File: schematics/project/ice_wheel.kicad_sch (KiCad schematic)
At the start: 2 parts, among them U1 OPA320xxDBV, U2 Teensy4.1

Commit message: Structure of schematics
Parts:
- removed U1: OPA320xxDBV, Package_TO_SOT_SMD:SOT-23-5, symbol Amplifier_Operational:OPA330xxDBV
- removed U2: Teensy4.1, teensy:Teensy41, symbol teensy:Teensy4.1
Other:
- added sheet Battery Management System (batmansys.kicad_sch)
- added sheet Bluetooth (bluetooth.kicad_sch)
- added sheet Misc (misc.kicad_sch)
- added sheet Motor Controller (motorController.kicad_sch)
- added sheet Prop Shield (propshield.kicad_sch)
- added sheet Teensy (teensy.kicad_sch)

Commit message: First steps with kicad structure -> kinda sucks
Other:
- sheet Prop Shield ports: added {I2C_Motion}, {SPI_PS}; removed I2C_Motion, SPI_propshield
- sheet Teensy ports: added {I2C_Motion}, {SPI_PS}; removed I2C_Motion, SPI_propshield

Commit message: some progress, dust slowly clears
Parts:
- added J1: Conn_01x02, Connector_JST:JST_SHL_SM02B-SHLS-TF_1x02-1MP_P1.00mm_Horizontal, symbol Connector_Generic:Conn_01x02
- added J2: Conn_01x02, symbol Connector_Generic:Conn_01x02
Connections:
- new net +48V: J2.1 (Pin_1)
- new net +5P: J1.1 (Pin_1)
- new net GND: J1.2 (Pin_2)
- new net GNDPWR: J2.2 (Pin_2)
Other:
- sheet Bluetooth ports: added Bluetooth; removed bt_rx, bt_tx
- sheet Motor Controller ports: added hallSensor; removed hallSensors
- sheet Teensy ports: added Bluetooth, footpad_a , hallSensor; removed bt_rx, bt_tx, hallSensors
- note added: "5V Input"

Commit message: small progress, angsthasen
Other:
- sheet Misc ports: added Speaker, poti_IN; removed none
- sheet Motor Controller ports: added throttle_pwm; removed throttle_a
- sheet Prop Shield ports: added Speaker; removed none
- sheet Teensy ports: added poti_IN; removed throttle_a
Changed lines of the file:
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@@
+    (stroke (width 0) (type default) (color 0 0 0 0))
+  )
+  (bus (pts (xy 161.29 73.66) (xy 161.29 80.01))
     (stroke (width 0) (type default) (color 0 0 0 0))
   )
@@
     (stroke (width 0) (type default) (color 0 0 0 0))
   )
-  (wire (pts (xy 153.67 107.95) (xy 166.37 107.95))
+  (wire (pts (xy 153.67 82.55) (xy 166.37 82.55))
+    (stroke (width 0) (type default) (color 0 0 0 0))
+  )
+  (bus (pts (xy 102.87 73.66) (xy 161.29 73.66))
     (stroke (width 0) (type default) (color 0 0 0 0))
   )
@@
     (stroke (width 0) (type default) (color 0 0 0 0))
   )
+  (bus (pts (xy 102.87 80.01) (xy 102.87 73.66))
+    (stroke (width 0) (type default) (color 0 0 0 0))
+  )
   (wire (pts (xy 69.85 27.94) (xy 69.85 30.48))
     (stroke (width 0) (type default) (color 0 0 0 0))
   )
+  (bus (pts (xy 96.52 80.01) (xy 102.87 80.01))
+    (stroke (width 0) (type default) (color 0 0 0 0))
+  )
   (wire (pts (xy 96.52 106.68) (xy 109.22 106.68))
     (stroke (width 0) (type default) (color 0 0 0 0))
@@
     (stroke (width 0) (type default) (color 0 0 0 0))
   )
+  (bus (pts (xy 161.29 80.01) (xy 166.37 80.01))
+    (stroke (width 0) (type default) (color 0 0 0 0))
+  )
+  (bus (pts (xy 153.67 107.95) (xy 166.37 107.95))
+    (stroke (width 0) (type default) (color 0 0 0 0))
+  )
   (wire (pts (xy 68.58 55.88) (xy 71.12 55.88))
     (stroke (width 0) (type default) (color 0 0 0 0))
   )
   (wire (pts (xy 72.39 25.4) (xy 69.85 25.4))
-    (stroke (width 0) (type default) (color 0 0 0 0))
-  )
-  (bus (pts (xy 153.67 80.01) (xy 166.37 80.01))
     (stroke (width 0) (type default) (color 0 0 0 0))
   )
@@
       (effects (font (size 1.27 1.27)) (justify right))
     )
+    (pin "Speaker" output (at 96.52 80.01 0)
+      (effects (font (size 1.27 1.27)) (justify right))
+    )
   )
   (sheet (at 166.37 127) (size 43.18 22.86) (fields_autoplaced)
@@
     )
   )
-  (sheet (at 166.37 77.47) (size 40.64 11.43) (fields_autoplaced)
+  (sheet (at 166.37 105.41) (size 40.64 11.43) (fields_autoplaced)
     (stroke (width 0.1524) (type solid) (color 0 0 0 0))
     (fill (color 0 0 0 0.0000))
-    (property "Sheet name" "Bluetooth" (id 0) (at 166.37 76.7584 0)
+    (property "Sheet name" "Bluetooth" (id 0) (at 166.37 104.6984 0)
       (effects (font (size 1.27 1.27)) (justify left bottom))
     )
-    (property "Sheet file" "bluetooth.kicad_sch" (id 1) (at 166.37 89.4846 0)
+    (property "Sheet file" "bluetooth.kicad_sch" (id 1) (at 166.37 117.4246 0)
       (effects (font (size 1.27 1.27)) (justify left top))
     )
-    (pin "Bluetooth" bidirectional (at 166.37 80.01 180)
+    (pin "Bluetooth" bidirectional (at 166.37 107.95 180)
       (effects (font (size 1.27 1.27)) (justify left))
     )
@@
       (effects (font (size 1.27 1.27)) (justify left))
     )
-    (pin "throttle_a" input (at 109.22 106.68 180)
-      (effects (font (size 1.27 1.27)) (justify left))
-    )
     (pin "lowPoBreak" input (at 109.22 119.38 180)
       (effects (font (size 1.27 1.27)) (justify left))
@@
       (effects (font (size 1.27 1.27)) (justify left))
     )
-    (pin "Bluetooth" bidirectional (at 153.67 80.01 0)
-      (effects (font (size 1.27 1.27)) (justify right))
-    )
-    (pin "footpad_a " input (at 153.67 107.95 0)
+    (pin "Bluetooth" bidirectional (at 153.67 107.95 0)
+      (effects (font (size 1.27 1.27)) (justify right))
+    )
+    (pin "footpad_a " input (at 153.67 82.55 0)
       (effects (font (size 1.27 1.27)) (justify right))
     )
     (pin "RS485_BMS" bidirectional (at 153.67 132.08 0)
       (effects (font (size 1.27 1.27)) (justify right))
+    )
+    (pin "poti_IN" input (at 109.22 106.68 180)
+      (effects (font (size 1.27 1.27)) (justify left))
     )
   )
@@
       (effects (font (size 1.27 1.27)) (justify right))
     )
-    (pin "throttle_a" input (at 96.52 106.68 0)
-      (effects (font (size 1.27 1.27)) (justify right))
-    )
     (pin "cruise" input (at 96.52 116.84 0)
       (effects (font (size 1.27 1.27)) (justify right))
@@
       (effects (font (size 1.27 1.27)) (justify right))
     )
-  )
-  (sheet (at 166.37 104.14) (size 25.4 10.16) (fields_autoplaced)
+    (pin "throttle_pwm" input (at 96.52 106.68 0)
+      (effects (font (size 1.27 1.27)) (justify right))
+    )
+  )
+  (sheet (at 166.37 77.47) (size 26.67 17.78) (fields_autoplaced)
     (stroke (width 0.1524) (type solid) (color 0 0 0 0))
     (fill (color 0 0 0 0.0000))
-    (property "Sheet name" "Misc" (id 0) (at 166.37 103.4284 0)
+    (property "Sheet name" "Misc" (id 0) (at 166.37 76.7584 0)
       (effects (font (size 1.27 1.27)) (justify left bottom))
     )
-    (property "Sheet file" "misc.kicad_sch" (id 1) (at 166.37 114.8846 0)
+    (property "Sheet file" "misc.kicad_sch" (id 1) (at 166.37 95.8346 0)
       (effects (font (size 1.27 1.27)) (justify left top))
     )
-    (pin "footpad_a " output (at 166.37 107.95 180)
+    (pin "footpad_a " output (at 166.37 82.55 180)
+      (effects (font (size 1.27 1.27)) (justify left))
+    )
+    (pin "Speaker" input (at 166.37 80.01 180)
+      (effects (font (size 1.27 1.27)) (justify left))
+    )
+    (pin "poti_IN" output (at 166.37 85.09 180)
       (effects (font (size 1.27 1.27)) (justify left))
     )
@@
       (reference "#PWR0137") (unit 1) (value "GND") (footprint "")
     )
+    (path "/a8032040-4653-49ee-95a3-c7cb36f467f5/990c3227-f66d-46f5-aa84-bd643388a276"
+      (reference "#PWR0138") (unit 1) (value "GND") (footprint "")
+    )
+    (path "/a8032040-4653-49ee-95a3-c7cb36f467f5/e02e4906-3c35-41b7-aaaa-ae3e3959c322"
+      (reference "#PWR0139") (unit 1) (value "+3V3") (footprint "")
+    )
+    (path "/a8032040-4653-49ee-95a3-c7cb36f467f5/f23605ae-8089-497b-a870-9c2ec8b93d03"
+      (reference "#PWR0140") (unit 1) (value "GND") (footprint "")
+    )
+    (path "/e60c338a-4f31-4486-88a3-b5454f96f251/5bd1a448-8ecc-4687-9ec0-737093a96f28"
+      (reference "#PWR0141") (unit 1) (value "GND") (footprint "")
+    )
+    (path "/e60c338a-4f31-4486-88a3-b5454f96f251/6c598751-03ec-42b5-8fe1-611876748d01"
+      (reference "#PWR0142") (unit 1) (value "+5V") (footprint "")
+    )
+    (path "/e60c338a-4f31-4486-88a3-b5454f96f251/c7b52073-3a92-4836-95ba-e712423fa30b"
+      (reference "#PWR0143") (unit 1) (value "GND") (footprint "")
+    )
+    (path "/e60c338a-4f31-4486-88a3-b5454f96f251/794c5c5e-371a-4787-81c1-a38c0fd636c6"
+      (reference "#PWR0144") (unit 1) (value "+5V") (footprint "")
+    )
+    (path "/e60c338a-4f31-4486-88a3-b5454f96f251/547e0894-6a74-49e9-9348-41865fbacb74"
+      (reference "#PWR0145") (unit 1) (value "GND") (footprint "")
+    )
+    (path "/e60c338a-4f31-4486-88a3-b5454f96f251/7bcb3274-ffad-47ba-85fa-1ec40074f0bc"
+      (reference "#PWR0146") (unit 1) (value "+5V") (footprint "")
+    )
     (path "/e170b43f-4cff-4505-8548-8011a1acf870/0a5cbc8c-d3cc-44f1-bc1d-4f5ea60978a2/654a37c9-46df-4b82-9933-5b4bab00a4da"
       (reference "C1") (unit 1) (value "C") (footprint "Capacitor_SMD:C_0603_1608Metric")
@@
       (reference "J2") (unit 1) (value "Conn_01x02") (footprint "")
     )
+    (path "/e60c338a-4f31-4486-88a3-b5454f96f251/c1085153-8f02-438d-ba95-d4b7d78aa733"
+      (reference "J3") (unit 1) (value "Conn_01x06") (footprint "")
+    )
+    (path "/e60c338a-4f31-4486-88a3-b5454f96f251/d6d0d868-e525-4399-bd4b-858390f2d3e6"
+      (reference "J4") (unit 1) (value "Conn_01x02") (footprint "")
+    )
     (path "/e170b43f-4cff-4505-8548-8011a1acf870/d87a0ee4-8016-40e3-98eb-7d78f313da4f"
       (reference "Q1") (unit 1) (value "BSS123") (footprint "Package_TO_SOT_SMD:SOT-23")
@@
     )
     (path "/e170b43f-4cff-4505-8548-8011a1acf870/8f7d1028-dc21-43d9-87a1-de994e1d134c"
-      (reference "R4") (unit 1) (value "R") (footprint "Resistor_SMD:R_0603_1608Metric")
+      (reference "R4") (unit 1) (value "1k") (footprint "Resistor_SMD:R_0603_1608Metric")
     )
     (path "/e170b43f-4cff-4505-8548-8011a1acf870/d7faf8fe-7d8a-426a-8274-194ddfcfaf5e"
-      (reference "R5") (unit 1) (value "R") (footprint "Resistor_SMD:R_0603_1608Metric")
+      (reference "R5") (unit 1) (value "1k") (footprint "Resistor_SMD:R_0603_1608Metric")
     )
     (path "/e170b43f-4cff-4505-8548-8011a1acf870/bcf35816-9bc9-4f6a-808b-350c85f525e7"
-      (reference "R6") (unit 1) (value "R") (footprint "Resistor_SMD:R_0603_1608Metric")
+      (reference "R6") (unit 1) (value "1k") (footprint "Resistor_SMD:R_0603_1608Metric")
     )
     (path "/e170b43f-4cff-4505-8548-8011a1acf870/cc39c052-37ed-400c-8ee6-c721ba66d828"
@@
       (reference "R13") (unit 1) (value "R") (footprint "Resistor_SMD:R_0603_1608Metric")
     )
+    (path "/e60c338a-4f31-4486-88a3-b5454f96f251/333792e1-5d2d-49b9-9ea6-0ab44501b72f"
+      (reference "RV1") (unit 1) (value "TC33X-1-203E") (footprint "Potentiometer_SMD:Potentiometer_Bourns_TC33X_Vertical")
+    )
+    (path "/e60c338a-4f31-4486-88a3-b5454f96f251/374f140d-5a1d-4c15-ab47-7f9415d6c4df"
+      (reference "RV2") (unit 1) (value "TC33X-1-203E") (footprint "Potentiometer_SMD:Potentiometer_Bourns_TC33X_Vertical")
+    )
+    (path "/e60c338a-4f31-4486-88a3-b5454f96f251/51914a10-e4f2-4520-870e-efe886085592"
+      (reference "RV3") (unit 1) (value "TC33X-1-203E") (footprint "Potentiometer_SMD:Potentiometer_Bourns_TC33X_Vertical")
+    )
     (path "/a8032040-4653-49ee-95a3-c7cb36f467f5/dd35ef3b-164d-4c70-932a-8e4d423737d2"

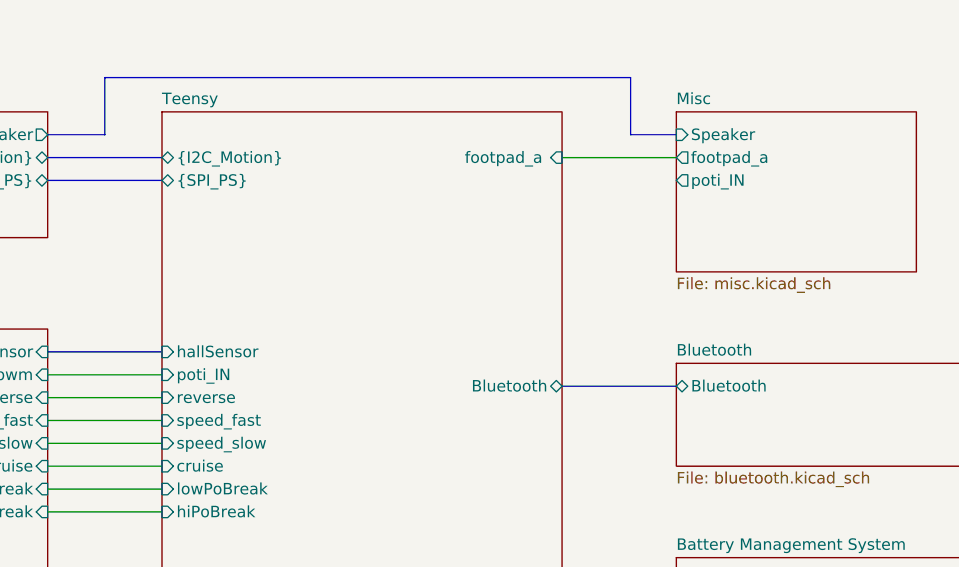
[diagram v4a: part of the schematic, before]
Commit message: Adding separate library, BT Module
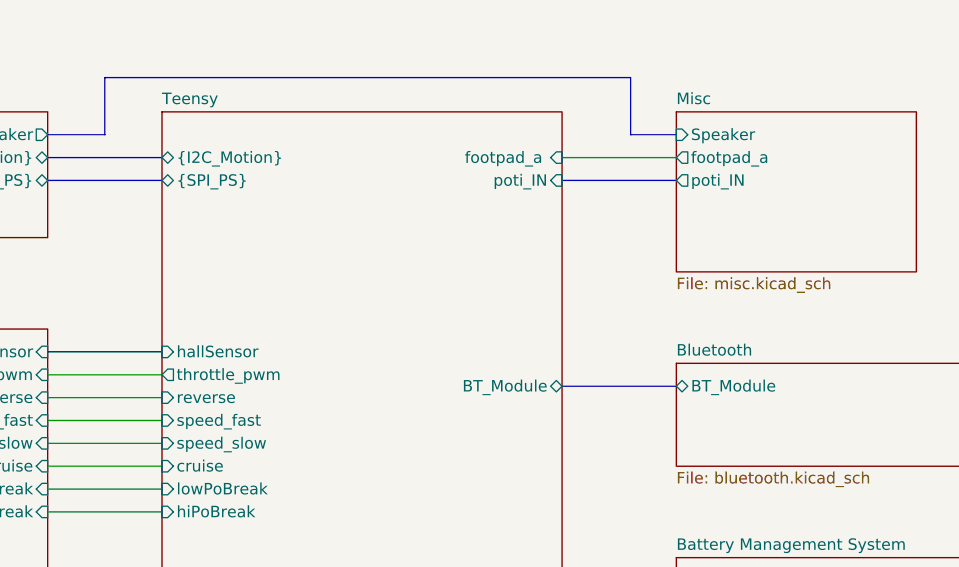
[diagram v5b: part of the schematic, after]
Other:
- sheet Bluetooth ports: added BT_Module; removed Bluetooth
- sheet Teensy ports: added BT_Module, throttle_pwm; removed Bluetooth

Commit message: random commit
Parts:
- J1: footprint Connector_JST:JST_SHL_SM02B-SHLS-TF_1x02-1MP_P1.00mm_Horizontal -> Connector_Phoenix_MSTB:PhoenixContact_MSTBA_2,5_2-G-5,08_1x02_P5.08mm_Horizontal
- J2: footprint (none) -> Connector_Phoenix_MSTB:PhoenixContact_MSTBA_2,5_2-G-5,08_1x02_P5.08mm_Horizontal
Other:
- sheet Misc ports: added analog_reserve, digital_reserve; removed none
- sheet Teensy ports: added analog_reserve, digital_reserve; removed none
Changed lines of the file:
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@@
+    (stroke (width 0) (type default) (color 0 0 0 0))
+  )
+  (bus (pts (xy 153.67 90.17) (xy 166.37 90.17))
     (stroke (width 0) (type default) (color 0 0 0 0))
   )
@@
   )
   (wire (pts (xy 69.85 25.4) (xy 69.85 22.86))
+    (stroke (width 0) (type default) (color 0 0 0 0))
+  )
+  (bus (pts (xy 153.67 87.63) (xy 166.37 87.63))
     (stroke (width 0) (type default) (color 0 0 0 0))
   )
@@
       (effects (font (size 1.27 1.27)) (justify left))
     )
-    (property "Footprint" "" (id 2) (at 77.47 25.4 0)
+    (property "Footprint" "Connector_Phoenix_MSTB:PhoenixContact_MSTBA_2,5_2-G-5,08_1x02_P5.08mm_Horizontal" (id 2) (at 77.47 25.4 0)
       (effects (font (size 1.27 1.27)) hide)
     )
@@
       (effects (font (size 1.27 1.27)) (justify left))
     )
-    (property "Footprint" "Connector_JST:JST_SHL_SM02B-SHLS-TF_1x02-1MP_P1.00mm_Horizontal" (id 2) (at 76.2 53.34 0)
+    (property "Footprint" "Connector_Phoenix_MSTB:PhoenixContact_MSTBA_2,5_2-G-5,08_1x02_P5.08mm_Horizontal" (id 2) (at 76.2 53.34 0)
       (effects (font (size 1.27 1.27)) hide)
     )
@@
       (effects (font (size 1.27 1.27)) (justify right))
     )
+    (pin "digital_reserve" bidirectional (at 153.67 87.63 0)
+      (effects (font (size 1.27 1.27)) (justify right))
+    )
+    (pin "analog_reserve" bidirectional (at 153.67 90.17 0)
+      (effects (font (size 1.27 1.27)) (justify right))
+    )
   )
   (sheet (at 67.31 101.6) (size 29.21 48.26) (fields_autoplaced)
@@
     )
     (pin "poti_IN" output (at 166.37 85.09 180)
+      (effects (font (size 1.27 1.27)) (justify left))
+    )
+    (pin "analog_reserve" bidirectional (at 166.37 90.17 180)
+      (effects (font (size 1.27 1.27)) (justify left))
+    )
+    (pin "digital_reserve" bidirectional (at 166.37 87.63 180)
       (effects (font (size 1.27 1.27)) (justify left))
     )
@@
     )
     (path "/e170b43f-4cff-4505-8548-8011a1acf870/fd47a1e5-df7e-4eee-a276-aa165209f13d"
-      (reference "#PWR?") (unit 1) (value "+48V") (footprint "")
+      (reference "#PWR0148") (unit 1) (value "+48V") (footprint "")
+    )
+    (path "/e60c338a-4f31-4486-88a3-b5454f96f251/787500e1-f92b-4a71-91ed-aadf5df66a1a"
+      (reference "#PWR0149") (unit 1) (value "GND") (footprint "")
+    )
+    (path "/e60c338a-4f31-4486-88a3-b5454f96f251/71b3e57e-4aff-4ae1-b69e-3eadce93f575"
+      (reference "#PWR0150") (unit 1) (value "GND") (footprint "")
     )
     (path "/e170b43f-4cff-4505-8548-8011a1acf870/0a5cbc8c-d3cc-44f1-bc1d-4f5ea60978a2/654a37c9-46df-4b82-9933-5b4bab00a4da"
@@
       (reference "D6") (unit 1) (value "D3V3S1U2LP1610-7") (footprint "Diode_SMD:D_0603_1608Metric_Pad1.05x0.95mm_HandSolder")
     )
+    (path "/e60c338a-4f31-4486-88a3-b5454f96f251/848f00ae-2b51-4a13-ba2b-b1d2cf17c1a6"
+      (reference "D7") (unit 1) (value "D3V3S1U2LP1610-7") (footprint "Diode_SMD:D_0603_1608Metric_Pad1.05x0.95mm_HandSolder")
+    )
+    (path "/e60c338a-4f31-4486-88a3-b5454f96f251/d1560112-0392-430e-8f8c-a61a68a9e881"
+      (reference "D8") (unit 1) (value "D3V3S1U2LP1610-7") (footprint "Diode_SMD:D_0603_1608Metric_Pad1.05x0.95mm_HandSolder")
+    )
     (path "/da0d5712-30e0-4d75-a17b-09a309cdb0af"
-      (reference "J1") (unit 1) (value "Conn_01x02") (footprint "Connector_JST:JST_SHL_SM02B-SHLS-TF_1x02-1MP_P1.00mm_Horizontal")
+      (reference "J1") (unit 1) (value "Conn_01x02") (footprint "Connector_Phoenix_MSTB:PhoenixContact_MSTBA_2,5_2-G-5,08_1x02_P5.08mm_Horizontal")
     )
     (path "/510d7d1a-ff03-4dad-9887-a4cfb9760797"
-      (reference "J2") (unit 1) (value "Conn_01x02") (footprint "")
+      (reference "J2") (unit 1) (value "Conn_01x02") (footprint "Connector_Phoenix_MSTB:PhoenixContact_MSTBA_2,5_2-G-5,08_1x02_P5.08mm_Horizontal")
     )
     (path "/e60c338a-4f31-4486-88a3-b5454f96f251/c1085153-8f02-438d-ba95-d4b7d78aa733"
-      (reference "J3") (unit 1) (value "Conn_01x06") (footprint "")
+      (reference "J3") (unit 1) (value "Conn_01x06") (footprint "Connector_JST:JST_SH_SM06B-SRSS-TB_1x06-1MP_P1.00mm_Horizontal")
     )
     (path "/e60c338a-4f31-4486-88a3-b5454f96f251/d6d0d868-e525-4399-bd4b-858390f2d3e6"
-      (reference "J4") (unit 1) (value "Conn_01x02") (footprint "")
+      (reference "J4") (unit 1) (value "Conn_01x02") (footprint "Connector_JST:JST_SHL_SM02B-SHLS-TF_1x02-1MP_P1.00mm_Horizontal")
     )
     (path "/e60c338a-4f31-4486-88a3-b5454f96f251/e31a5680-510d-4c8b-a1a2-e25dc53ad7a6"
-      (reference "J5") (unit 1) (value "Conn_01x03") (footprint "")
+      (reference "J5") (unit 1) (value "Conn_01x03") (footprint "Connector_JST:JST_SH_SM03B-SRSS-TB_1x03-1MP_P1.00mm_Horizontal")
     )
     (path "/e60c338a-4f31-4486-88a3-b5454f96f251/c3347128-bd85-463f-99a3-a170653c0a78"
-      (reference "J6") (unit 1) (value "Conn_01x03") (footprint "")
+      (reference "J6") (unit 1) (value "Conn_01x03") (footprint "Connector_JST:JST_SH_SM03B-SRSS-TB_1x03-1MP_P1.00mm_Horizontal")
     )
     (path "/e60c338a-4f31-4486-88a3-b5454f96f251/59eb5277-81e5-44a0-8d7f-fbaaca11b3ac"
-      (reference "J7") (unit 1) (value "Conn_01x03") (footprint "")
+      (reference "J7") (unit 1) (value "Conn_01x03") (footprint "Connector_JST:JST_SH_SM03B-SRSS-TB_1x03-1MP_P1.00mm_Horizontal")
     )
     (path "/e170b43f-4cff-4505-8548-8011a1acf870/37d09877-6887-4f3d-80c6-a82cacc84ce0"
@@
     )
     (path "/7ec07ddd-7068-43d0-9fd5-859900c03ac0/ef9e4a68-783a-4a05-ae16-76eb42d17d85"
-      (reference "J9") (unit 1) (value "Conn_01x03") (footprint "")
+      (reference "J9") (unit 1) (value "Conn_01x03") (footprint "Connector_JST:JST_SH_SM03B-SRSS-TB_1x03-1MP_P1.00mm_Horizontal")
+    )
+    (path "/e170b43f-4cff-4505-8548-8011a1acf870/87be6bbd-26ab-4c15-97d2-790a4b9e56c6"
+      (reference "J10") (unit 1) (value "Conn_01x05") (footprint "Connector_JST:JST_SH_SM05B-SRSS-TB_1x05-1MP_P1.00mm_Horizontal")
     )
     (path "/e170b43f-4cff-4505-8548-8011a1acf870/d87a0ee4-8016-40e3-98eb-7d78f313da4f"
